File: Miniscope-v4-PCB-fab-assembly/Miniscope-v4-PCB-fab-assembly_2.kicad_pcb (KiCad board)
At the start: 6 copper layers, 35.5 x 45 mm, 109 parts, among them J1 Conn_01x01, J1 Conn_01x14, J1 Conn_01x20, J10 Conn_01x05, J16 Conn_01x20_Female, J2 Conn_01x01, J2 Conn_01x14, J3 Conn_01x01, J4 Conn_01x01, J5 Conn_01x01, J6 Conn_01x01, J7 Conn_01x01, J8 Conn_01x05, J9 Conn_01x01, Q1 MMBT3904LP-7B, U1 ATmega328-MU, U1 DS90UB933-Q1, U1 LMV321IDCKR, U1 MAX14574EWL+, U2 NOIP1SN0480A, U2 TPL0102-100RUCR, U3 LTC3218, U3 SiT_2.5mmx2mm, U3 TLV7103318DSER

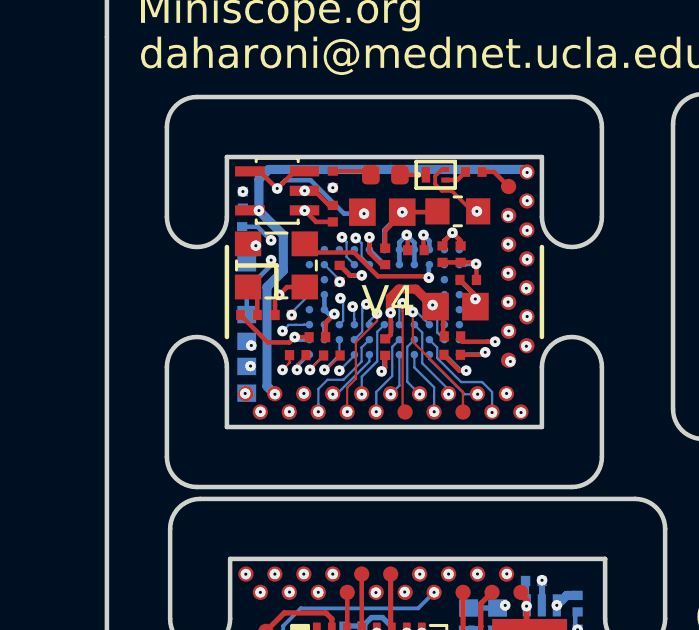
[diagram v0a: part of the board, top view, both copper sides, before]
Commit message: Minor name changes
Updates:

*1.8k,47.7k and LED on the Python480 boards now renamed to include the correct part number name for PnP feeder configuration matching

*Corrected a few capacitors on the serializer board to include their correct part number
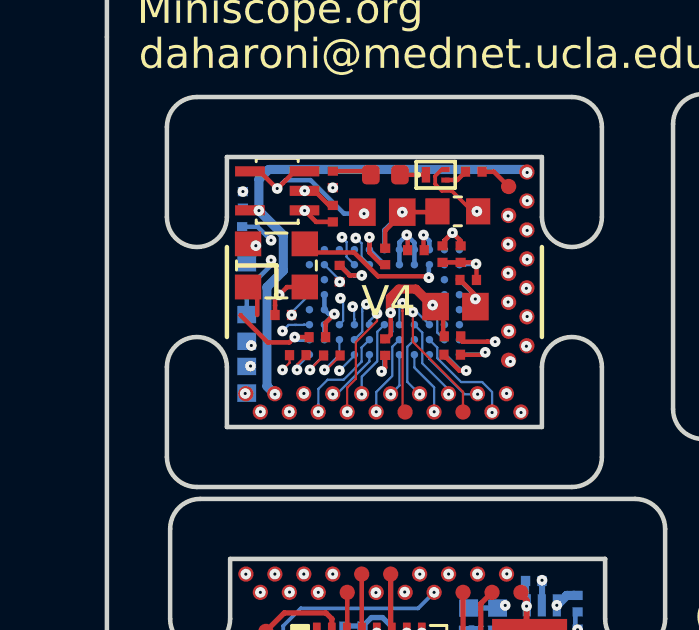
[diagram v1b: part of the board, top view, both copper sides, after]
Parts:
- removed the R2 at (84.0, 109.7)
- C18, C23: value GRM155R60J475ME47D -> GRM155R60J475ME87D
- C26: value GRJ155R60J106ME11D -> GRM155R60J106ME15D
- D1: value LED_Small_ALT -> VLMS1500-GS08
- R1: value 1.8K -> ERJ-1GNF1801C
- R1: value MMBT3904LP-7B -> ERJ-1GEF2001C
- R2, R3: value ERJ-1GEF1022C -> DNL
- R3: value 47.7K -> ERJ-1GNF4752C
- R3, R4: value ERJ-1GEF1002C -> ERJ-1GEF1022C
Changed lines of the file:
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@@
-(kicad_pcb (version 20171130) (host pcbnew "(5.1.0)-1")
+(kicad_pcb (version 20171130) (host pcbnew "(5.1.2)-1")
   (general
     (thickness 0.7874)
@@
     (tracks 1130)
     (zones 0)
-    (modules 109)
+    (modules 108)
     (nets 117)
   )
@@
     (44 Edge.Cuts user)
     (45 Margin user)
-    (46 B.CrtYd user)
-    (47 F.CrtYd user)
+    (46 B.CrtYd user hide)
+    (47 F.CrtYd user hide)
     (48 B.Fab user hide)
     (49 F.Fab user hide)
@@
       (effects (font (size 1 1) (thickness 0.1)))
     )
-    (fp_text value 47.7K (at 0 0 180) (layer F.Fab)
+    (fp_text value ERJ-1GNF4752C (at 0 0 180) (layer F.Fab)
       (effects (font (size 1.2 1.2) (thickness 0.12)))
     )
@@
   )
   (module .Resistor:R_0201_0603Metric_ERJ_L (layer F.Cu)
-    (at 83.96294 109.68418 180)
-    (descr "Resistor, Chip; 0.60 mm L X 0.30 mm W X 0.26 mm H body")
-    (attr smd)
-    (fp_text reference R2 (at 0 0 180) (layer F.Fab) hide
-      (effects (font (size 1 1) (thickness 0.1)))
-    )
-    (fp_text value DNL (at 0 0 180) (layer F.Fab)
-      (effects (font (size 1.2 1.2) (thickness 0.12)))
-    )
-    (fp_line (start 0 -0.135) (end 0 0.135) (layer F.CrtYd) (width 0.05))
-    (fp_line (start 0.135 0) (end -0.135 0) (layer F.CrtYd) (width 0.05))
-    (fp_circle (center 0 0) (end 0 0.1013) (layer F.CrtYd) (width 0.05))
-    (fp_line (start 0.53 0.27) (end -0.53 0.27) (layer F.CrtYd) (width 0.05))
-    (fp_line (start 0.53 -0.27) (end 0.53 0.27) (layer F.CrtYd) (width 0.05))
-    (fp_line (start -0.53 -0.27) (end 0.53 -0.27) (layer F.CrtYd) (width 0.05))
-    (fp_line (start -0.53 0.27) (end -0.53 -0.27) (layer F.CrtYd) (width 0.05))
-    (fp_line (start 0.32 0.17) (end -0.32 0.17) (layer F.Fab) (width 0.12))
-    (fp_line (start 0.32 -0.17) (end 0.32 0.17) (layer F.Fab) (width 0.12))
-    (fp_line (start -0.32 -0.17) (end 0.32 -0.17) (layer F.Fab) (width 0.12))
-    (fp_line (start -0.32 0.17) (end -0.32 -0.17) (layer F.Fab) (width 0.12))
-    (fp_line (start 0.3 0.15) (end -0.3 0.15) (layer Dwgs.User) (width 0.025))
-    (fp_line (start 0.3 -0.15) (end 0.3 0.15) (layer Dwgs.User) (width 0.025))
-    (fp_line (start -0.3 -0.15) (end 0.3 -0.15) (layer Dwgs.User) (width 0.025))
-    (fp_line (start -0.3 0.15) (end -0.3 -0.15) (layer Dwgs.User) (width 0.025))
-    (fp_line (start 0.3 0.15) (end 0.15 0.15) (layer Dwgs.User) (width 0.025))
-    (fp_line (start 0.3 -0.15) (end 0.3 0.15) (layer Dwgs.User) (width 0.025))
-    (fp_line (start 0.15 -0.15) (end 0.3 -0.15) (layer Dwgs.User) (width 0.025))
-    (fp_line (start 0.15 0.15) (end 0.15 -0.15) (layer Dwgs.User) (width 0.025))
-    (fp_line (start -0.3 -0.15) (end -0.15 -0.15) (layer Dwgs.User) (width 0.025))
-    (fp_line (start -0.3 0.15) (end -0.3 -0.15) (layer Dwgs.User) (width 0.025))
-    (fp_line (start -0.15 0.15) (end -0.3 0.15) (layer Dwgs.User) (width 0.025))
-    (fp_line (start -0.15 -0.15) (end -0.15 0.15) (layer Dwgs.User) (width 0.025))
-    (fp_text user %R (at 1.905 -1.1684 180) (layer F.SilkS) hide
-      (effects (font (size 0.5 0.5) (thickness 0.05)))
-    )
-    (pad 2 smd rect (at 0.275 0 180) (size 0.31 0.34) (layers F.Cu F.Paste F.Mask)
-      (net 6 +3V3))
-    (pad 1 smd rect (at -0.275 0 180) (size 0.31 0.34) (layers F.Cu F.Paste F.Mask)
-      (net 13 "Net-(R2-Pad1)"))
-    (model ${KICAD_AHARONI_LAB}/Modules/Resistor.pretty/R_0201_0603Metric_ERJ_L.STEP
-      (at (xyz 0 0 0))
-      (scale (xyz 1 1 1))
-      (rotate (xyz -90 0 0))
-    )
-  )
-  (module .Resistor:R_0201_0603Metric_ERJ_L (layer F.Cu)
     (at 86.75694 105.16298 270)
     (descr "Resistor, Chip; 0.60 mm L X 0.30 mm W X 0.26 mm H body")
@@
       (effects (font (size 1 1) (thickness 0.1)))
     )
-    (fp_text value 1.8K (at 0 0 270) (layer F.Fab)
+    (fp_text value ERJ-1GNF1801C (at 0 0 270) (layer F.Fab)
       (effects (font (size 1.2 1.2) (thickness 0.12)))
     )
@@
       (effects (font (size 1 1) (thickness 0.15)))
     )
-    (fp_text value LED_Small_ALT (at 0 1.17 180) (layer F.Fab)
+    (fp_text value VLMS1500-GS08 (at 0 1.17 180) (layer F.Fab)
       (effects (font (size 1 1) (thickness 0.15)))
     )
@@
       (effects (font (size 1 1) (thickness 0.1)))
     )
-    (fp_text value ERJ-1GEF1022C (at 0 0) (layer F.Fab)
+    (fp_text value DNL (at 0 0) (layer F.Fab)
       (effects (font (size 1.2 1.2) (thickness 0.12)))
     )
@@
       (effects (font (size 1 1) (thickness 0.1)))
     )
-    (fp_text value ERJ-1GEF1022C (at 0 0 270) (layer F.Fab)
+    (fp_text value DNL (at 0 0 270) (layer F.Fab)
       (effects (font (size 1.2 1.2) (thickness 0.12)))
     )
@@
       (effects (font (size 1 1) (thickness 0.1)) (justify mirror))
     )
-    (fp_text value GRJ155R60J106ME11D (at 0 0) (layer B.Fab)
+    (fp_text value GRM155R60J106ME15D (at 0 0) (layer B.Fab)
       (effects (font (size 1.2 1.2) (thickness 0.12)) (justify mirror))
     )
@@
       (effects (font (size 1 1) (thickness 0.1)) (justify mirror))
     )
-    (fp_text value ERJ-1GEF1002C (at 0 0 90) (layer B.Fab)
+    (fp_text value ERJ-1GEF1022C (at 0 0 90) (layer B.Fab)
       (effects (font (size 1.2 1.2) (thickness 0.12)) (justify mirror))
     )
@@
       (effects (font (size 1 1) (thickness 0.1)) (justify mirror))
     )
-    (fp_text value GRM155R60J475ME47D (at 0 0 90) (layer B.Fab)
+    (fp_text value GRM155R60J475ME87D (at 0 0 90) (layer B.Fab)
       (effects (font (size 1.2 1.2) (thickness 0.12)) (justify mirror))
     )
@@
       (effects (font (size 1 1) (thickness 0.1)) (justify mirror))
     )
-    (fp_text value GRM155R60J475ME47D (at 0 0 180) (layer B.Fab)
+    (fp_text value GRM155R60J475ME87D (at 0 0 180) (layer B.Fab)
       (effects (font (size 1.2 1.2) (thickness 0.12)) (justify mirror))
     )
@@
       (effects (font (size 1 1) (thickness 0.1)) (justify mirror))
     )
-    (fp_text value MMBT3904LP-7B (at 0 0 270) (layer B.Fab)
+    (fp_text value ERJ-1GEF2001C (at 0 0 270) (layer B.Fab)
       (effects (font (size 1.2 1.2) (thickness 0.12)) (justify mirror))
     )
@@
       (effects (font (size 1 1) (thickness 0.1)) (justify mirror))
     )
-    (fp_text value ERJ-1GEF1002C (at 0 0 180) (layer B.Fab)
+    (fp_text value ERJ-1GEF1022C (at 0 0 180) (layer B.Fab)
       (effects (font (size 1.2 1.2) (thickness 0.12)) (justify mirror))
     )
